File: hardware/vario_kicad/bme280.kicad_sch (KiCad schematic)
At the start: 7 parts, among them U2 BME280

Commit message: update footprints, add LSE oscillator
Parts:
- R1, R2: footprint (none) -> Resistor_SMD:R_0402_1005Metric
- TP1, TP2: footprint (none) -> TestPoint:TestPoint_Pad_D1.0mm
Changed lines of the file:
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@@
 			)
 		)
-		(property "Footprint" ""
+		(property "Footprint" "Resistor_SMD:R_0402_1005Metric"
 			(at 163.322 88.9 90)
 			(effects
@@
 			)
 		)
-		(property "Footprint" ""
+		(property "Footprint" "TestPoint:TestPoint_Pad_D1.0mm"
 			(at 190.5 101.6 0)
 			(effects
@@
 			)
 		)
-		(property "Footprint" ""
+		(property "Footprint" "TestPoint:TestPoint_Pad_D1.0mm"
 			(at 187.96 96.52 0)
 			(effects
@@
 			)
 		)
-		(property "Footprint" ""
+		(property "Footprint" "Resistor_SMD:R_0402_1005Metric"
 			(at 151.892 88.9 90)
 			(effects

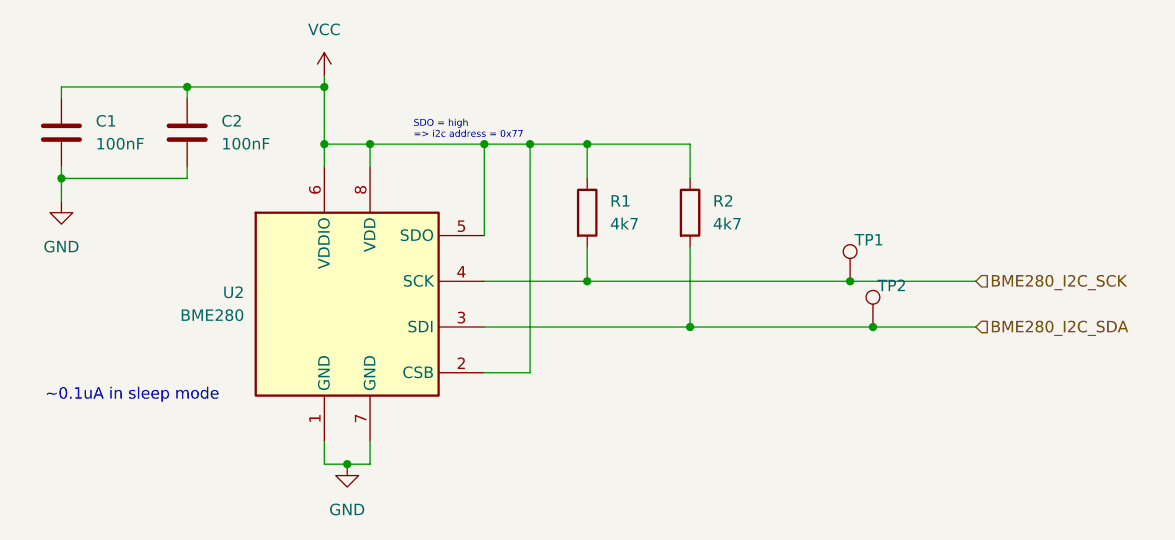
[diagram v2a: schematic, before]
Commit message: add missing footprints
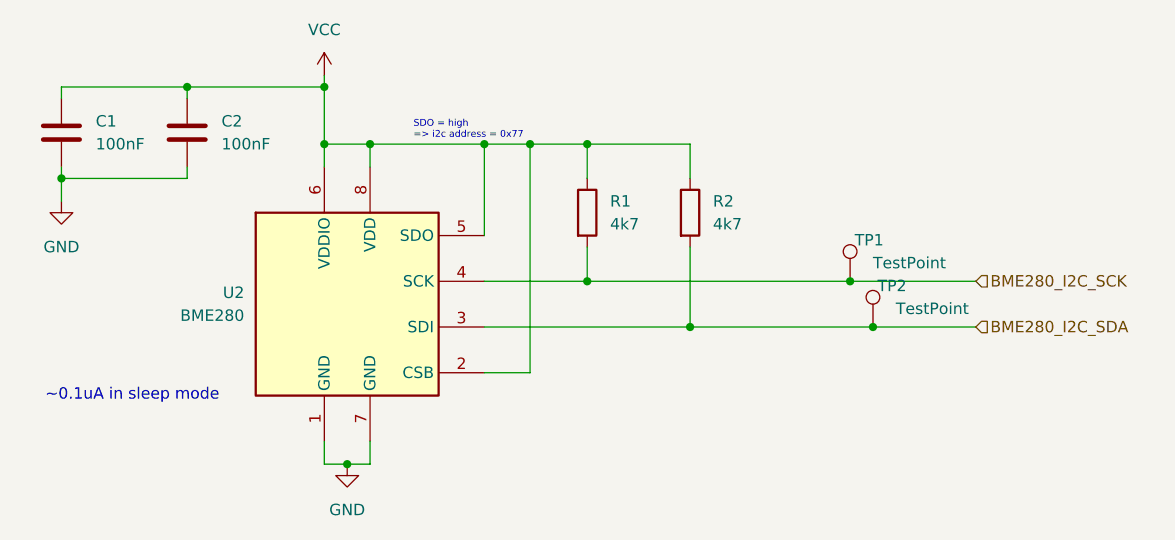
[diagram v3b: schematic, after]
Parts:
- TP1, TP2: value ~ -> TestPoint
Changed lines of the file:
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@@
 			)
 		)
-		(property "Value" "~"
+		(property "Value" "TestPoint"
 			(at 187.96 99.5679 0)
 			(effects
@@
 			)
 		)
-		(property "Value" "~"
+		(property "Value" "TestPoint"
 			(at 185.42 94.4879 0)
 			(effects

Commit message: remove useless test points
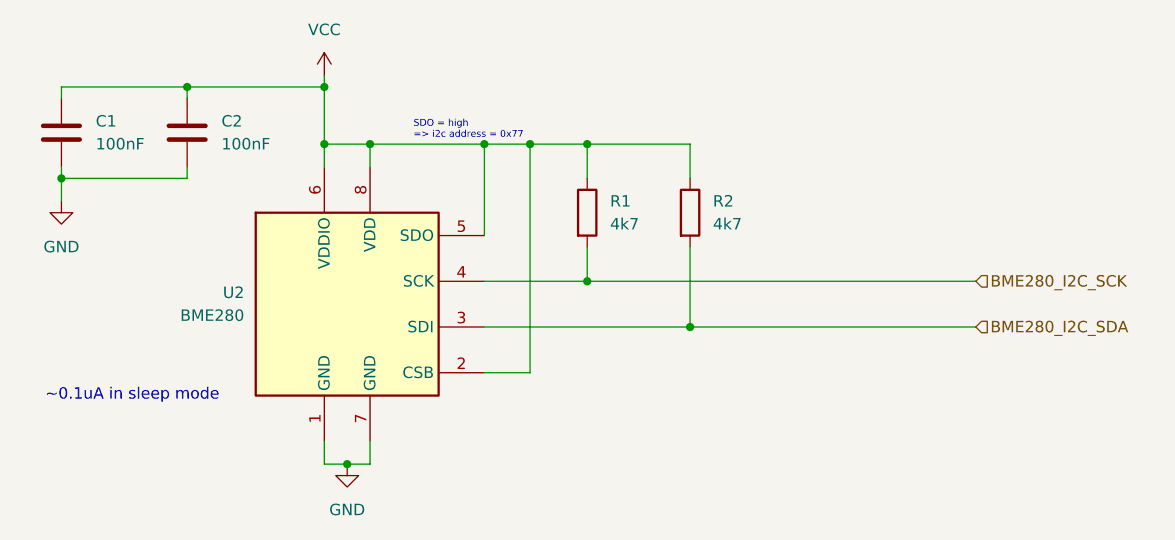
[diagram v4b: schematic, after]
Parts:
- removed TP1, TP2: TestPoint, TestPoint:TestPoint_Pad_D1.0mm, symbol Connector:TestPoint
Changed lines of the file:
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@@
-	)
-	(junction
-		(at 182.88 96.52)
-		(diameter 0)
-		(color 0 0 0 0)
 	)
 	(junction
@@
 	)
 	(junction
-		(at 185.42 101.6)
-		(diameter 0)
-		(color 0 0 0 0)
-	)
-	(junction
 		(at 95.25 85.09)
 		(diameter 0)
@@
 	(wire
 		(pts
-			(xy 196.85 96.52) (xy 182.88 96.52)
-		)
-		(stroke
-			(width 0)
-			(type default)
-		)
-	)
-	(wire
-		(pts
 			(xy 165.1 92.71) (xy 165.1 101.6)
 		)
@@
 	(wire
 		(pts
-			(xy 165.1 101.6) (xy 185.42 101.6)
+			(xy 165.1 101.6) (xy 196.85 101.6)
 		)
 		(stroke
@@
 	(wire
 		(pts
-			(xy 153.67 96.52) (xy 182.88 96.52)
+			(xy 153.67 96.52) (xy 196.85 96.52)
 		)
 		(stroke
@@
 		(pts
 			(xy 124.46 83.82) (xy 124.46 81.28)
-		)
-		(stroke
-			(width 0)
-			(type default)
-		)
-	)
-	(wire
-		(pts
-			(xy 196.85 101.6) (xy 185.42 101.6)
 		)
 		(stroke
@@
 	)
 	(symbol
-		(lib_id "Connector:TestPoint")
-		(at 185.42 101.6 0)
-		(unit 1)
-		(exclude_from_sim no)
-		(in_bom yes)
-		(on_board yes)
-		(dnp no)
-		(property "Reference" "TP2"
-			(at 185.928 97.028 0)
-			(effects
-				(font
-					(size 1.27 1.27)
-				)
-				(justify left)
-			)
-		)
-		(property "Value" "TestPoint"
-			(at 187.96 99.5679 0)
-			(effects
-				(font
-					(size 1.27 1.27)
-				)
-				(justify left)
-			)
-		)
-		(property "Footprint" "TestPoint:TestPoint_Pad_D1.0mm"
-			(at 190.5 101.6 0)
-			(effects
-				(font
-					(size 1.27 1.27)
-				)
-				(hide yes)
-			)
-		)
-		(property "Datasheet" "~"
-			(at 190.5 101.6 0)
-			(effects
-				(font
-					(size 1.27 1.27)
-				)
-				(hide yes)
-			)
-		)
-		(property "Description" "test point"
-			(at 185.42 101.6 0)
-			(effects
-				(font
-					(size 1.27 1.27)
-				)
-				(hide yes)
-			)
-		)
-		(property "Sim.Pins" ""
-			(at 185.42 101.6 0)
-			(effects
-				(font
-					(size 1.27 1.27)
-				)
-				(hide yes)
-			)
-		)
-		(pin "1"
-		)
-		(instances
-			(project "vario_kicad"
-				(path "/50389aff-b244-451e-8e3a-c5addd2215e1/a2acba3f-1e31-48a4-807d-9523c9d04b72"
-					(reference "TP2")
-					(unit 1)
-				)
-			)
-		)
-	)
-	(symbol
 		(lib_id "power:GND")
 		(at 95.25 87.63 0)
@@
 					(unit 1)
 				)
-			)
-		)
-	)
-	(symbol
-		(lib_id "Connector:TestPoint")
-		(at 182.88 96.52 0)
-		(unit 1)
-		(exclude_from_sim no)
-		(in_bom yes)
-		(on_board yes)
-		(dnp no)
-		(property "Reference" "TP1"
-			(at 183.388 91.948 0)
-			(effects
-				(font
-					(size 1.27 1.27)
-				)
-				(justify left)
-			)
-		)
-		(property "Value" "TestPoint"
-			(at 185.42 94.4879 0)
-			(effects
-				(font
-					(size 1.27 1.27)
-				)
-				(justify left)
-			)
-		)
-		(property "Footprint" "TestPoint:TestPoint_Pad_D1.0mm"
-			(at 187.96 96.52 0)
-			(effects
-				(font
-					(size 1.27 1.27)
-				)
-				(hide yes)
-			)
-		)
-		(property "Datasheet" "~"
-			(at 187.96 96.52 0)
-			(effects
-				(font
-					(size 1.27 1.27)
-				)
-				(hide yes)
-			)
-		)
-		(property "Description" "test point"
-			(at 182.88 96.52 0)
-			(effects
-				(font
-					(size 1.27 1.27)
-				)
-				(hide yes)
-			)
-		)
-		(property "Sim.Pins" ""
-			(at 182.88 96.52 0)
-			(effects
-				(font
-					(size 1.27 1.27)
-				)
-				(hide yes)
-			)
-		)
-		(pin "1"
-		)
-		(instances
-			(project "vario_kicad"
-				(path "/50389aff-b244-451e-8e3a-c5addd2215e1/a2acba3f-1e31-48a4-807d-9523c9d04b72"
-					(reference "TP1")
-					(unit 1)
-				)

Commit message: use 0402 instead of 0603 for almost all caps
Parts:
- C1, C2: footprint Capacitor_SMD:C_0603_1608Metric -> Capacitor_SMD:C_0402_1005Metric
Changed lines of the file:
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@@
 			)
 		)
-		(property "Footprint" "Capacitor_SMD:C_0603_1608Metric"
+		(property "Footprint" "Capacitor_SMD:C_0402_1005Metric"
 			(at 96.2152 83.82 0)
 			(effects
@@
 			)
 		)
-		(property "Footprint" "Capacitor_SMD:C_0603_1608Metric"
+		(property "Footprint" "Capacitor_SMD:C_0402_1005Metric"
 			(at 110.1852 83.82 0)
 			(effects
